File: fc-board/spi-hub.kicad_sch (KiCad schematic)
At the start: 22 parts, among them J15 BCS-110-L-D-TE, U10 LTC2983ILX-PBF

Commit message: some updates
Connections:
- net CH17: no longer C22.1, J15.20, JP10.2 (B), JP11.2 (B), JP12.2 (B), JP13.2 (B), JP14.2 (B), JP15.2 (B), JP8.2 (B), JP9.2 (B), R37.2, U10.35 (CH20)
- new net CH20: C22.1, J15.20, JP10.2 (B), JP11.2 (B), JP12.2 (B), JP13.2 (B), JP14.2 (B), JP15.2 (B), JP8.2 (B), JP9.2 (B), R37.2, U10.35 (CH20)
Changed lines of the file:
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@@
-		)
-	)
-	(label "CH20"
-		(at 163.83 69.85 180)
-		(effects
-			(font
-				(size 1.27 1.27)
-			)
-			(justify right bottom)
 		)
 	)

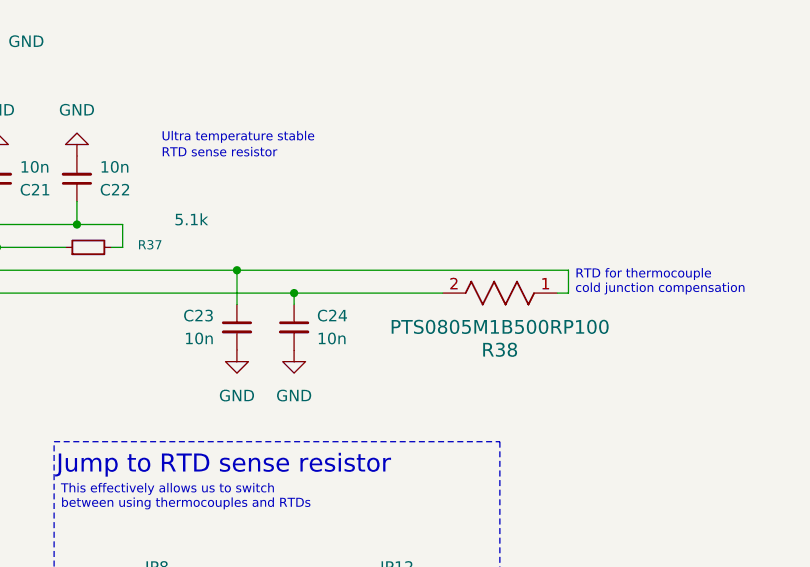
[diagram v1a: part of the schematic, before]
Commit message: fc board: some updates but not passing DRC
(disconnected items)
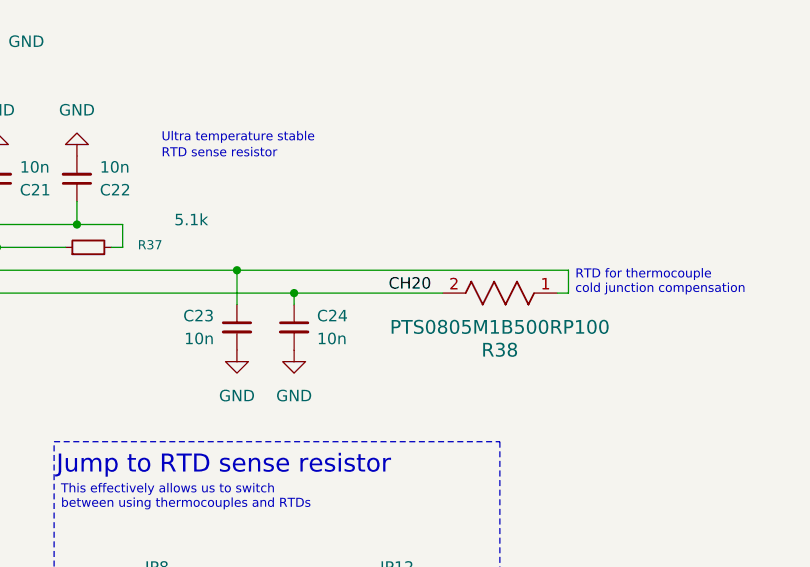
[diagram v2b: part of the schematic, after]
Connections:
- net CH20 is gone; now on net CH17: C22.1, J15.20, JP10.2 (B), JP11.2 (B), JP12.2 (B), JP13.2 (B), JP14.2 (B), JP15.2 (B), JP8.2 (B), JP9.2 (B), R37.2, U10.35 (CH20)
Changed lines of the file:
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@@
+	)
+	(label "CH20"
+		(at 163.83 69.85 180)
+		(effects
+			(font
+				(size 1.27 1.27)
+			)
+			(justify right bottom)
+		)
 	)
 	(label "CH20"
